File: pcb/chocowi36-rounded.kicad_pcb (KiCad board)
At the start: 2 copper layers, 113.2 x 88.5 mm, 27 parts, among them SW10 SW_Push, SW11 SW_Push, SW12 SW_Push, SW14 SW_Push, SW15 SW_Push, SW16 SW_Push, SW17 SW_Push, SW18 SW_Push, SW19 SW_Push, SW2 SW_Push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

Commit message: small changes + update doc
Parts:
- removed H2, H3: MountingHole, itsdmd:MountingHole_1.6mm_M1.4
- added ?: , , F.Cu at (103.9, 105.0)
- added ?: , , F.Cu at (150.6, 51.0)
- H1, H4: footprint itsdmd:MountingHole_1.6mm_M1.4 -> itsdmd:MountingHole_2.2mm_M2
- moved H1 13.3 mm to (90.5, 55.0)
- moved H4 12.9 mm to (178.6, 111.3)
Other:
- board size 113.2 x 88.5 mm -> 113.1 x 88.3 mm
- board text added: "by itsdmd"
- board text added: "chocowi36"

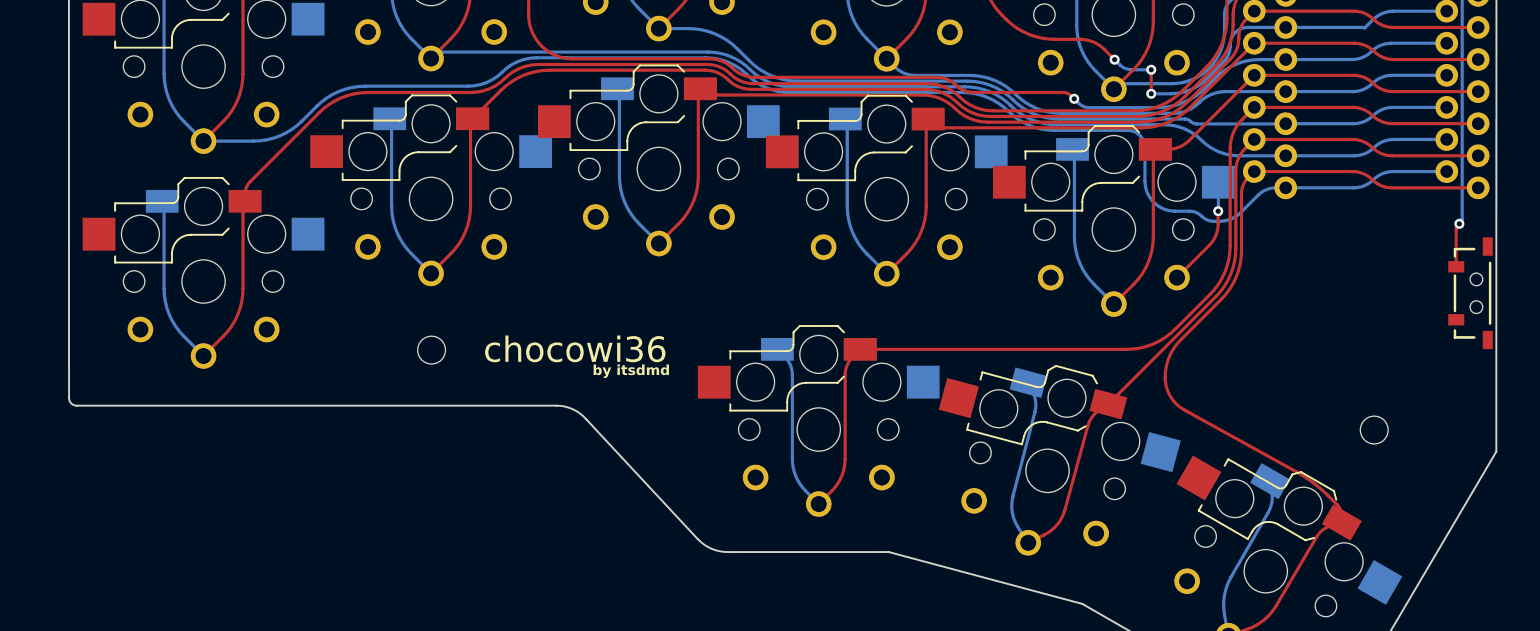
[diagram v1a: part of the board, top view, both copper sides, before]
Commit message: adjust thumb cluster
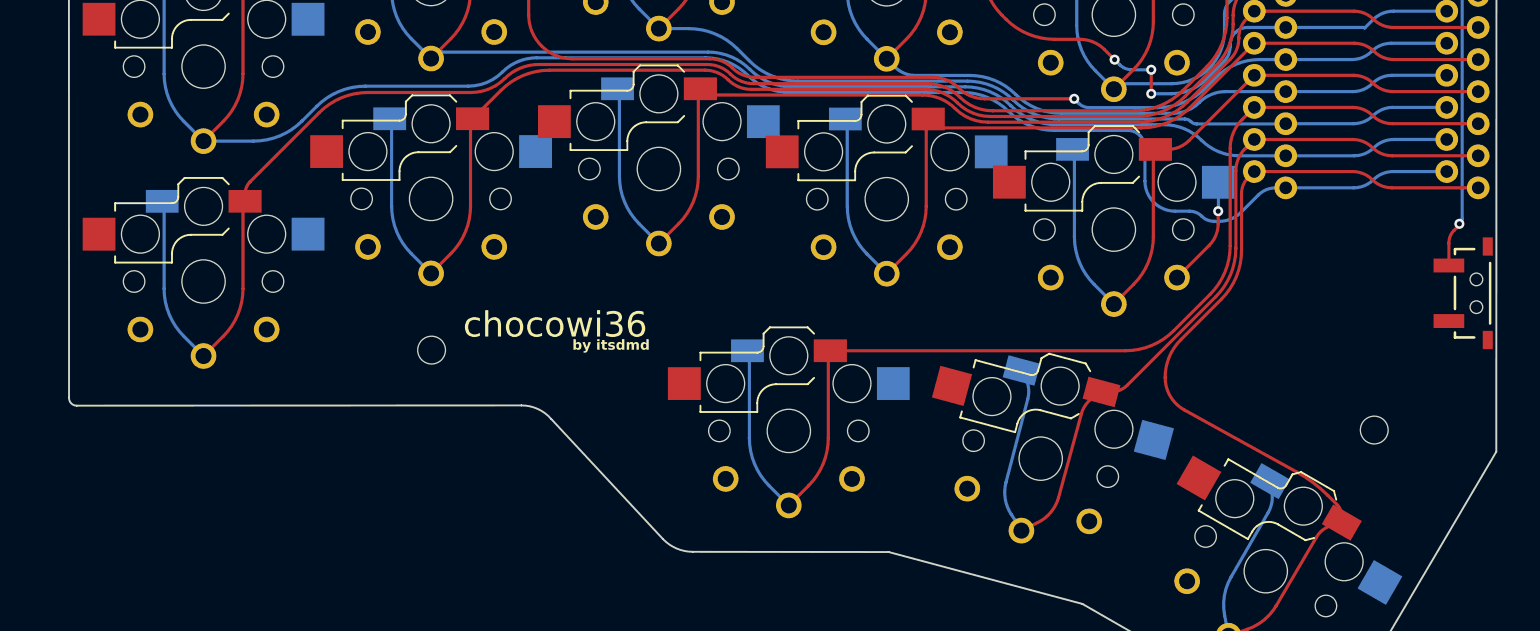
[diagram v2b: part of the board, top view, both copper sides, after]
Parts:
- moved SW19 2.37 mm to (132.2, 111.4)
- moved SW20 1.11 mm to (152.1, 113.6)
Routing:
- net Switch19: track 89.8 -> 92.3 mm
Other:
- outline, holes or cut-outs redrawn
